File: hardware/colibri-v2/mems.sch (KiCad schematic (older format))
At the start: 9 parts, among them U1 L3GD20, U2 LSM303D

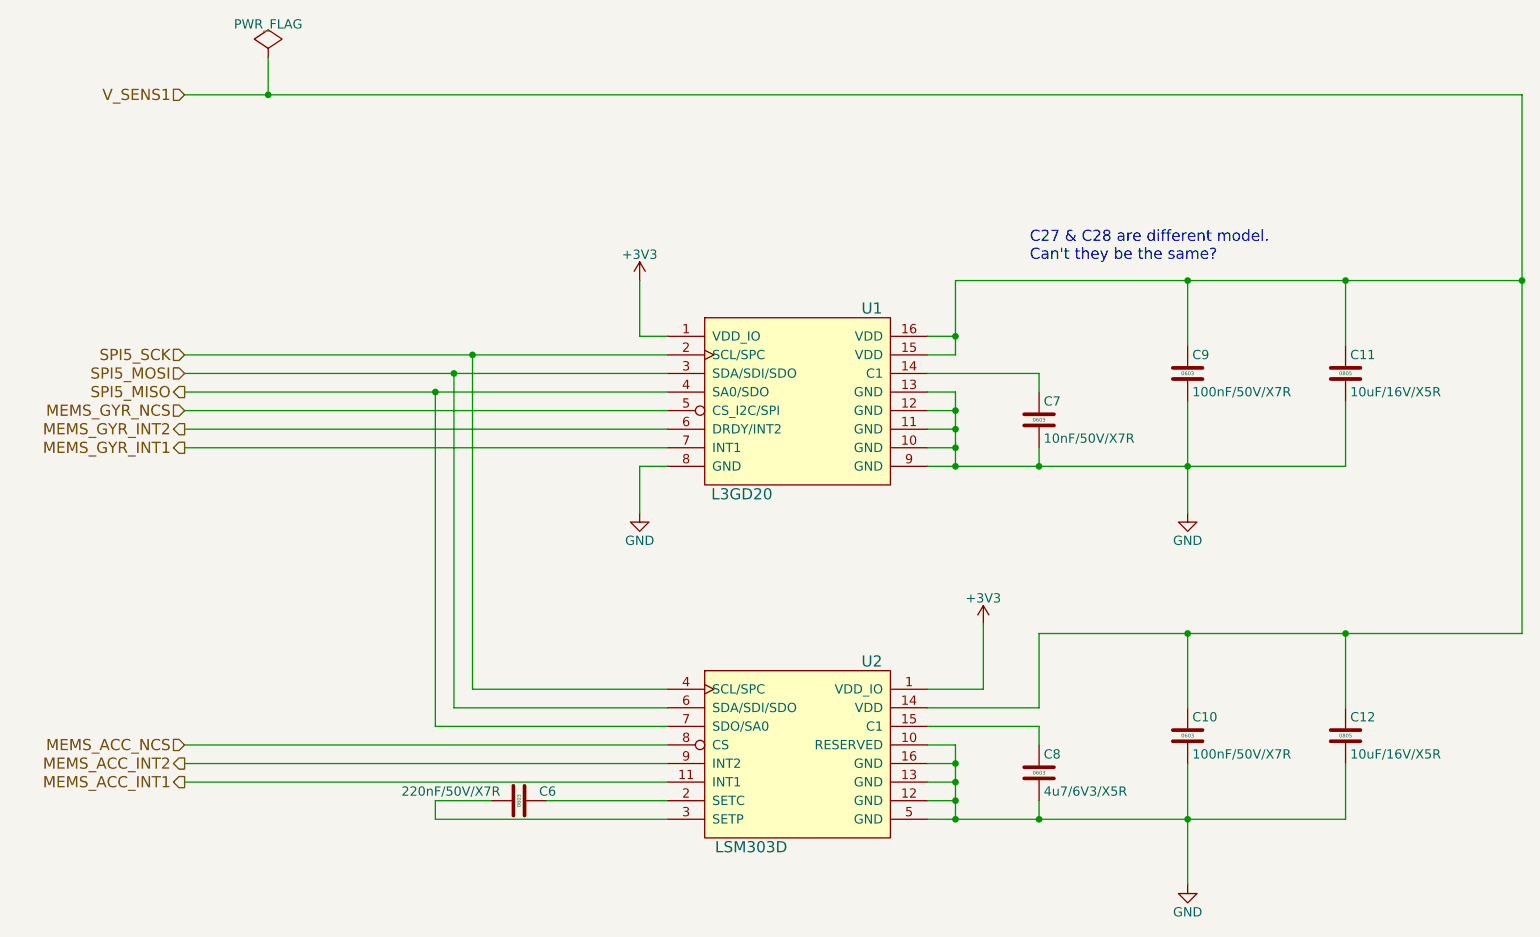
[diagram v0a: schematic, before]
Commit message: Added C to power inputs for MEMS and pressure. Work on board to board connector.
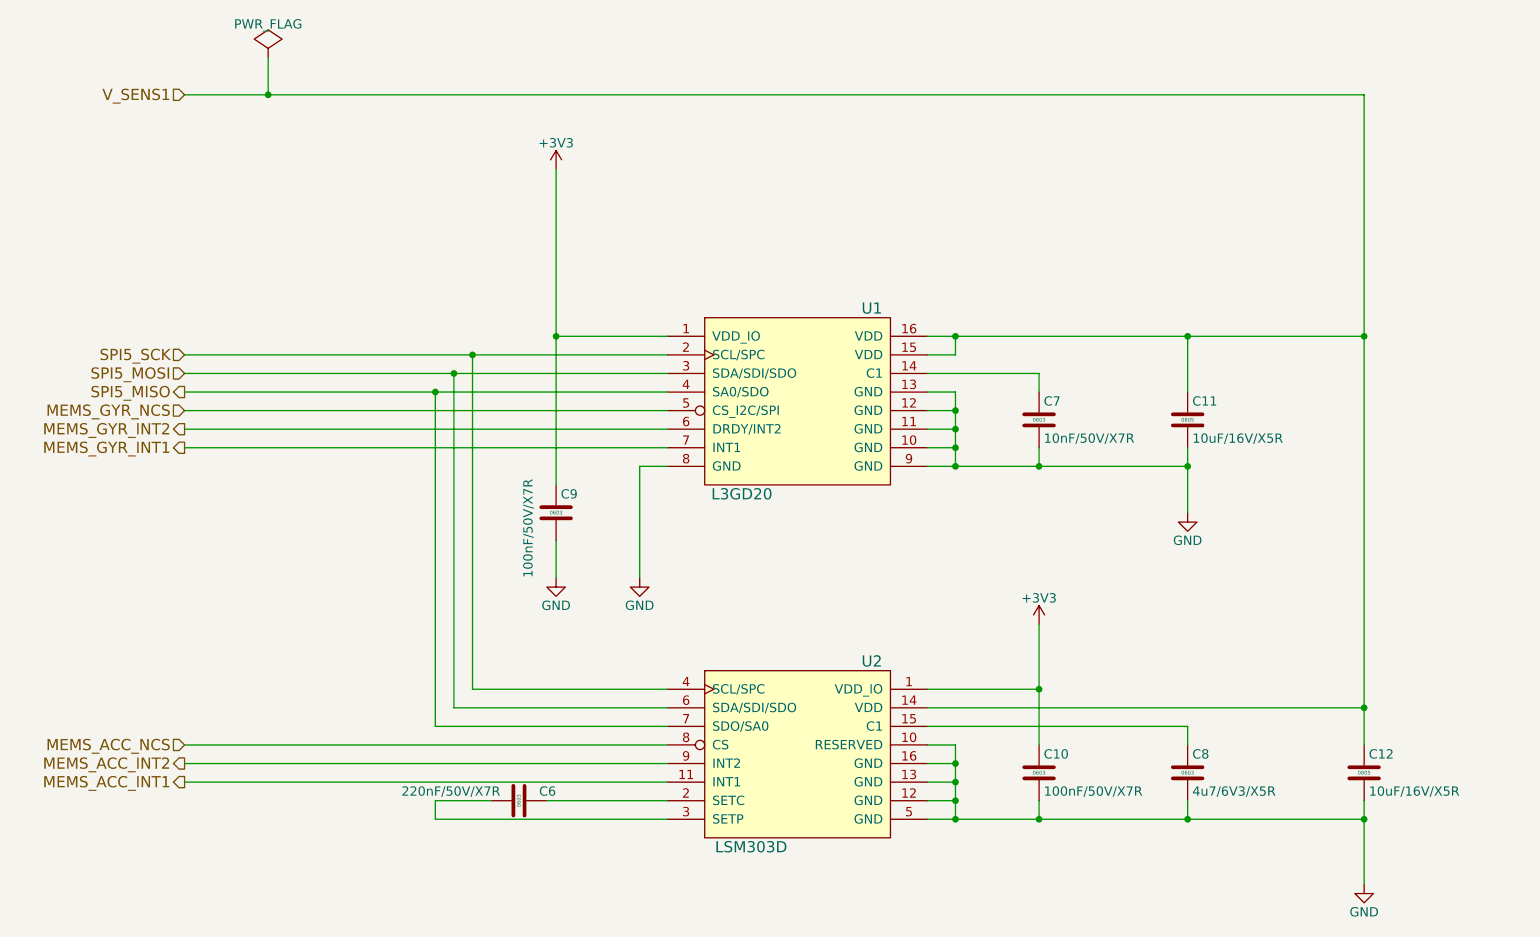
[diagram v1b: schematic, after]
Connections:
- net +3V3: now also C10.1, C9.1
- net V_SENS1: no longer C10.1, C9.1
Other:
- note removed: "C27 & C28 are different model.\nCan't they be the same?"
- moved on the sheet: C10, C11, C12, C8, C9

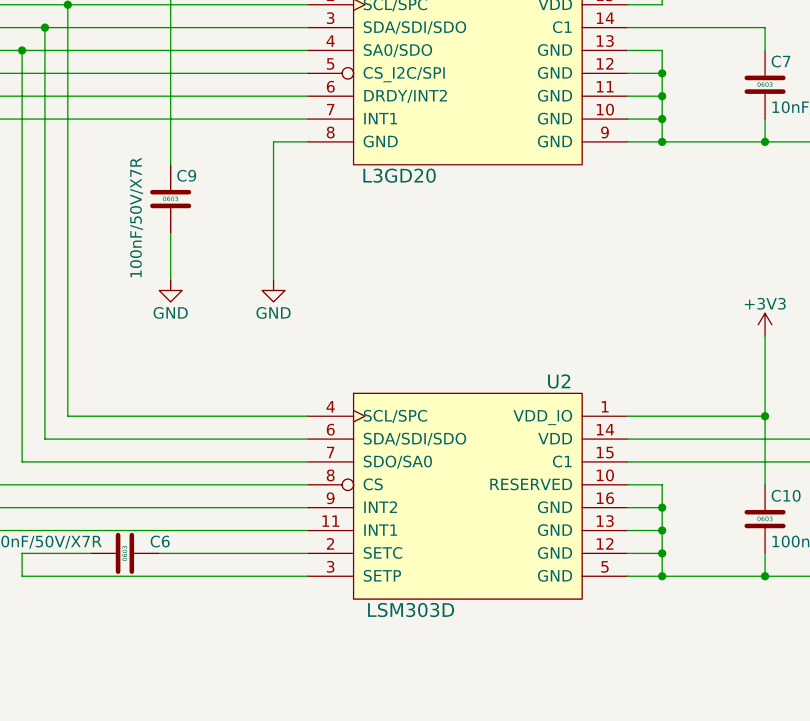
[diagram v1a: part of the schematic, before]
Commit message: Added footprints
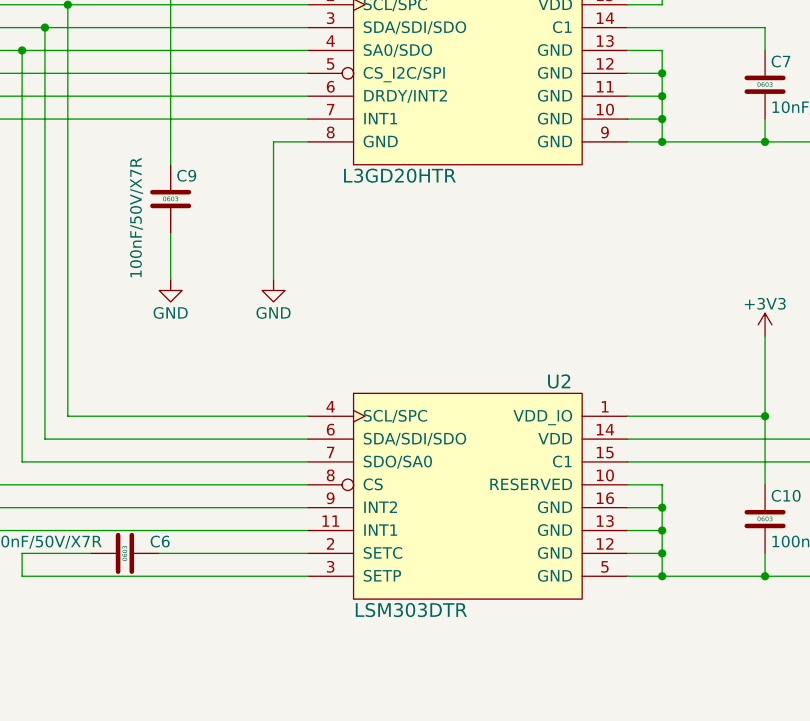
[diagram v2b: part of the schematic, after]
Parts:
- U1: value L3GD20 -> L3GD20HTR; Part (none) -> 497-13931-1-ND; Provider (none) -> Digikey
- U2: value LSM303D -> LSM303DTR; Part (none) -> 497-13819-1-ND; Provider (none) -> Digikey
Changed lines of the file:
@@
 P 4800 3350
 F 0 "U1" H 5200 3850 60  0000 C CNN
-F 1 "L3GD20" H 4500 2850 60  0000 C CNN
+F 1 "L3GD20HTR" H 4500 2850 60  0000 C CNN
 F 2 "" H 4800 3500 60  0001 C CNN
 F 3 "" H 4800 3500 60  0000 C CNN
+F 4 "497-13931-1-ND" H 4800 3350 60  0001 C CNN "Part"
+F 5 "Digikey" H 4800 3350 60  0001 C CNN "Provider"
 	1    4800 3350
 	1    0    0    -1
@@
 P 4800 5250
 F 0 "U2" H 5200 5750 60  0000 C CNN
-F 1 "LSM303D" H 4550 4750 60  0000 C CNN
+F 1 "LSM303DTR" H 4550 4750 60  0000 C CNN
 F 2 "" H 4800 5400 60  0001 C CNN
 F 3 "" H 4800 5400 60  0000 C CNN
+F 4 "497-13819-1-ND" H 4800 5250 60  0001 C CNN "Part"
+F 5 "Digikey" H 4800 5250 60  0001 C CNN "Provider"
 	1    4800 5250
 	1    0    0    -1

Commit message: Assigned footprints
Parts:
- U1, U2: footprint (none) -> Sigmadrone:LGA16-3MM_LONG_PADS
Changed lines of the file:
@@
 F 0 "U1" H 5200 3850 60  0000 C CNN
 F 1 "L3GD20HTR" H 4500 2850 60  0000 C CNN
-F 2 "" H 4800 3500 60  0001 C CNN
+F 2 "Sigmadrone:LGA16-3MM_LONG_PADS" H 4800 3500 60  0001 C CNN
 F 3 "" H 4800 3500 60  0000 C CNN
 F 4 "497-13931-1-ND" H 4800 3350 60  0001 C CNN "Part"
@@
 F 0 "U2" H 5200 5750 60  0000 C CNN
 F 1 "LSM303DTR" H 4550 4750 60  0000 C CNN
-F 2 "" H 4800 5400 60  0001 C CNN
+F 2 "Sigmadrone:LGA16-3MM_LONG_PADS" H 4800 5400 60  0001 C CNN
 F 3 "" H 4800 5400 60  0000 C CNN
 F 4 "497-13819-1-ND" H 4800 5250 60  0001 C CNN "Part"
